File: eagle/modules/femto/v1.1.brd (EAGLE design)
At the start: 50.5 x 25.4 mm, 25 parts, among them IC1 MEGA8-AI, J1 RJ12RIGHTANGLE-I2C, J2 RJ12RIGHTANGLE-I2C

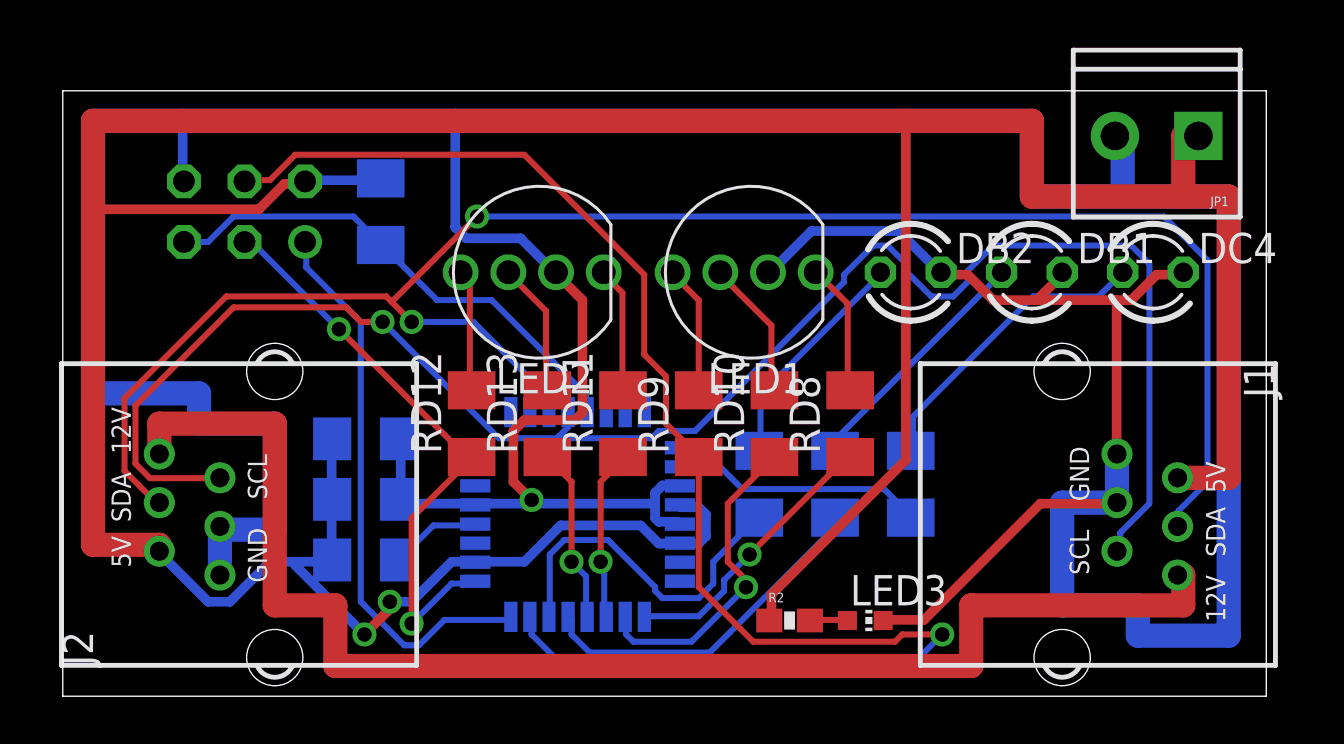
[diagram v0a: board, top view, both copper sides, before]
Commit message: Finish Femto I2C version 1.0
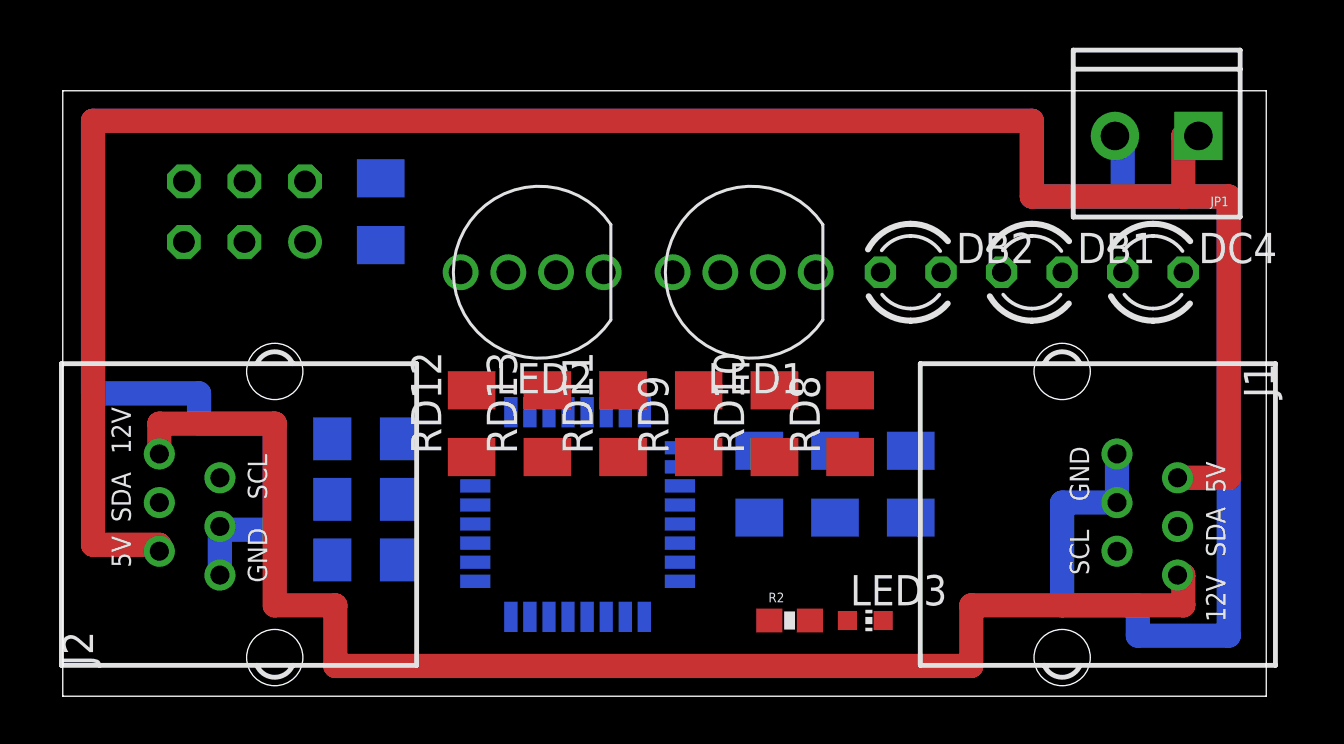
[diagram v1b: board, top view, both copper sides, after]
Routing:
- net GND: track 199.7 -> 118.1 mm, vias 1 -> 0
- net SDA: track 75.2 -> 0.00 mm, vias 2 -> 0
- net +5V: track 162.0 -> 88.7 mm, vias 2 -> 0
- net SCL: track 72.7 -> 0.00 mm, vias 1 -> 0
- net MOSI: track 63.7 -> 0.00 mm, vias 1 -> 0
- net SCK: track 24.7 -> 0.00 mm, vias 2 -> 0
- net MISO: track 23.7 -> 0.00 mm
- net RESET: track 21.2 -> 0.00 mm
- net N$18: track 14.8 -> 0.00 mm
- net N$19: track 14.7 -> 0.00 mm
- net D6: track 13.4 -> 0.00 mm, vias 1 -> 0
- net N$23: track 12.8 -> 0.00 mm
- net D5: track 11.7 -> 0.00 mm, vias 1 -> 0
- net N$11: track 10.9 -> 0.00 mm
- net N$40: track 10.4 -> 0.00 mm
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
